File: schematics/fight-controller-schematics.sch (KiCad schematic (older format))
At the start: 13 parts

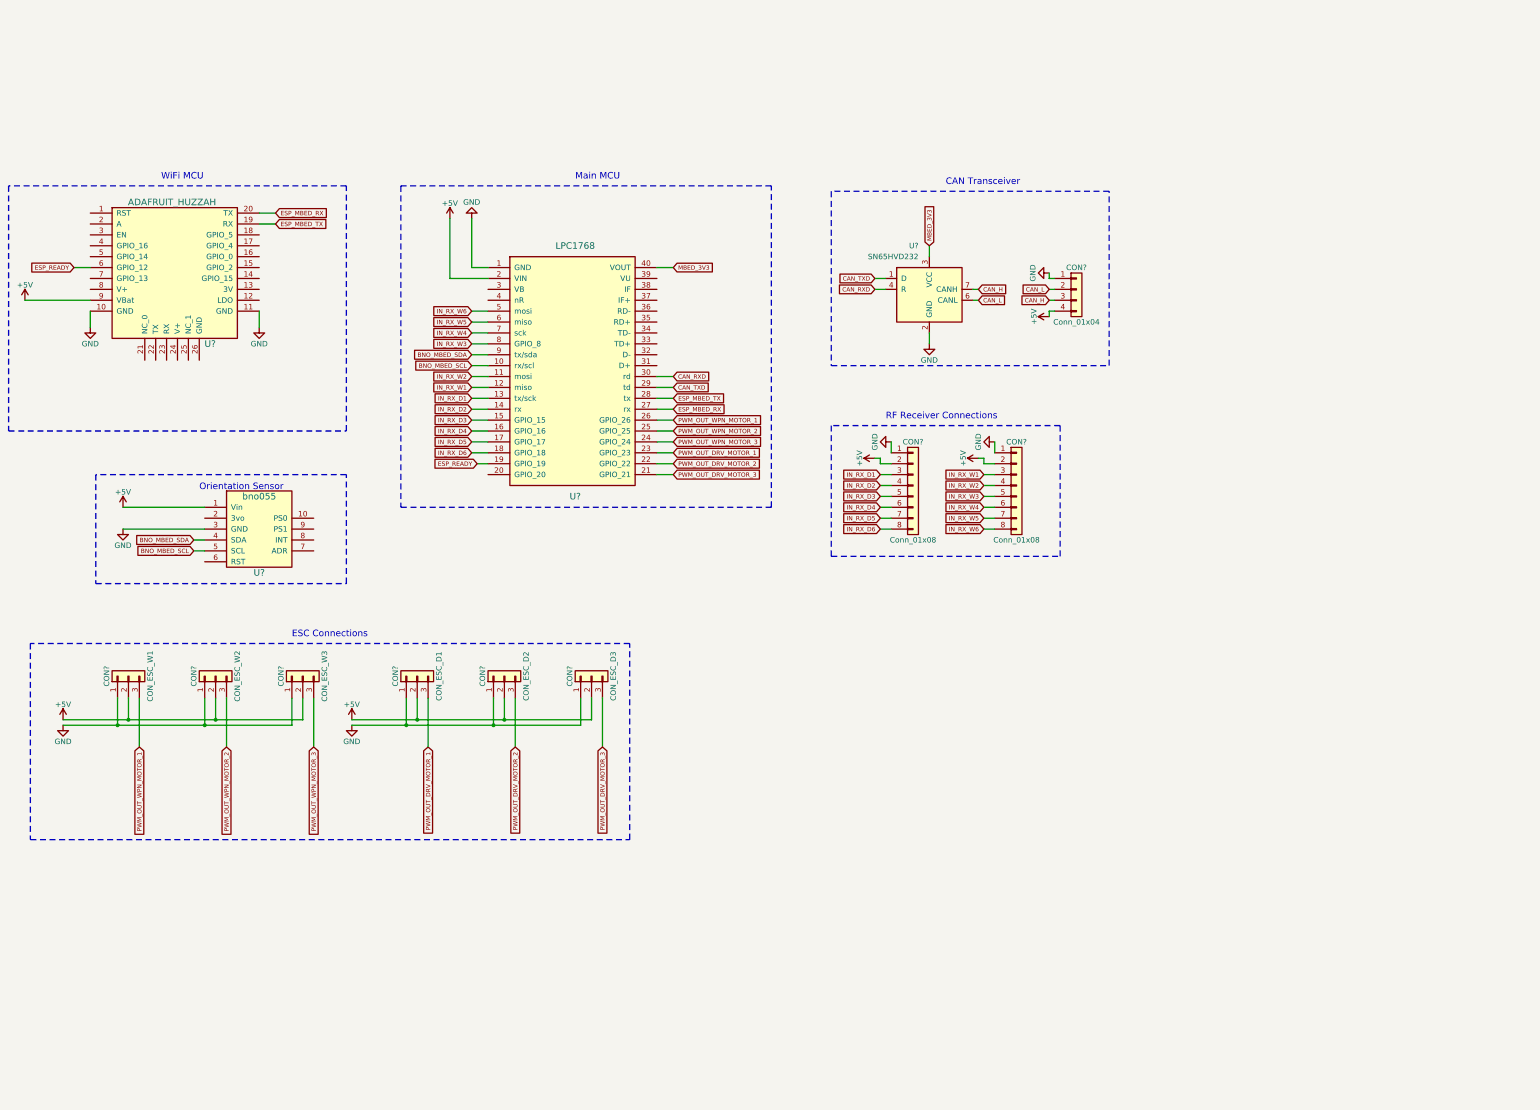
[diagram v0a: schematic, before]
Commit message: Started v2.x work, integrating developement boards into PCB.
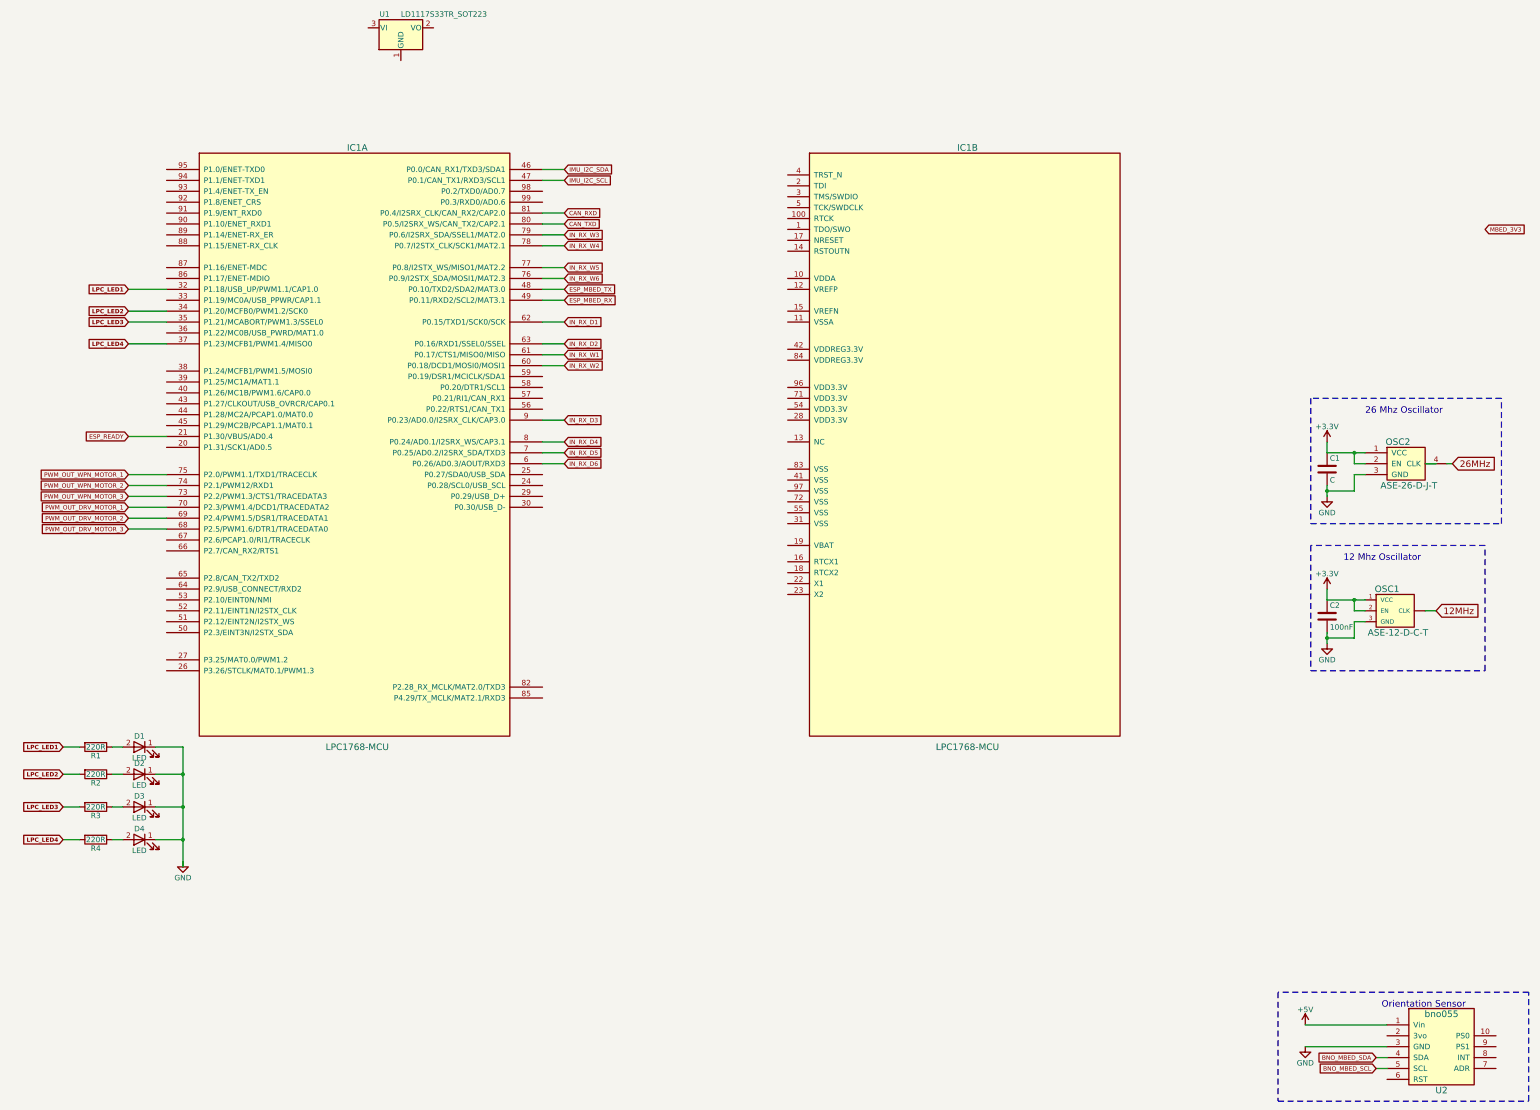
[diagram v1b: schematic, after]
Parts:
- removed CON?: Conn_01x04, Connectors_JST:JST_PH_S4B-PH-K_04x2.00mm_Angled, symbol Conn_01x04
- removed CON? (x2): Conn_01x08, Connectors_JST:JST_SH_SM08B-SRSS-TB_08x1.00mm_Angled, symbol Conn_01x08
- removed CON?: CON_ESC_W1, mbed:Pin_Header_Angled_3x01_Pitch2.54mm, symbol Conn_01x03
- removed CON?: CON_ESC_W2, mbed:Pin_Header_Angled_3x01_Pitch2.54mm, symbol Conn_01x03
- removed CON?: CON_ESC_W3, mbed:Pin_Header_Angled_3x01_Pitch2.54mm, symbol Conn_01x03
- removed CON?: CON_ESC_D1, mbed:Pin_Header_Angled_3x01_Pitch2.54mm, symbol Conn_01x03
- removed CON?: CON_ESC_D2, mbed:Pin_Header_Angled_3x01_Pitch2.54mm, symbol Conn_01x03
- removed CON?: CON_ESC_D3, mbed:Pin_Header_Angled_3x01_Pitch2.54mm, symbol Conn_01x03
- removed U?: LPC1768, Triforce_Fight_Controller:lpc1768, symbol LPC1768
- removed U?: ADAFRUIT_HUZZAH, Triforce_Fight_Controller:ESP8266, symbol ADAFRUIT_HUZZAH
- removed U?: SN65HVD232, Triforce_Fight_Controller:SOIC-8_3.9x4.9mm_Pitch1.27mm, symbol SN65HVD232
- added C1: C, symbol C
- added C2: 100nF, symbol C
- added D1, D2, D3, D4: LED, symbol LED
- added IC1: LPC1768-MCU, symbol LPC1768-MCU
- added OSC1: ASE-12-D-C-T, symbol ASE-12-D-C-T
- added OSC2: ASE-26-D-J-T, symbol ASE-26-D-J-T
- added R1, R2, R3, R4: 220R, symbol R
- added U1: LD1117S33TR_SOT223, TO_SOT_Packages_SMD:SOT-223-3Lead_TabPin2, symbol LD1117S33TR_SOT223
- gave numbers to parts that had none: 1
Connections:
- net labels added: +3.3V, 12MHz, 26MHz, IMU_I2C_SCL, IMU_I2C_SDA, LPC_LED1, LPC_LED2, LPC_LED3, LPC_LED4
- net labels removed: CAN_H, CAN_L
- wire segments 94 -> 65
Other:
- note added: "12 Mhz Oscillator"
- note added: "26 Mhz Oscillator"
- note removed: "CAN Transceiver"
- note removed: "ESC Connections"
- note removed: "Main MCU"
- note removed: "RF Receiver Connections"
- note removed: "WiFi MCU"
- moved on the sheet: U2
